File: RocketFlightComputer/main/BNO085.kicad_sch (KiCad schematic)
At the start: 12 parts, among them Y3 32.768kHz

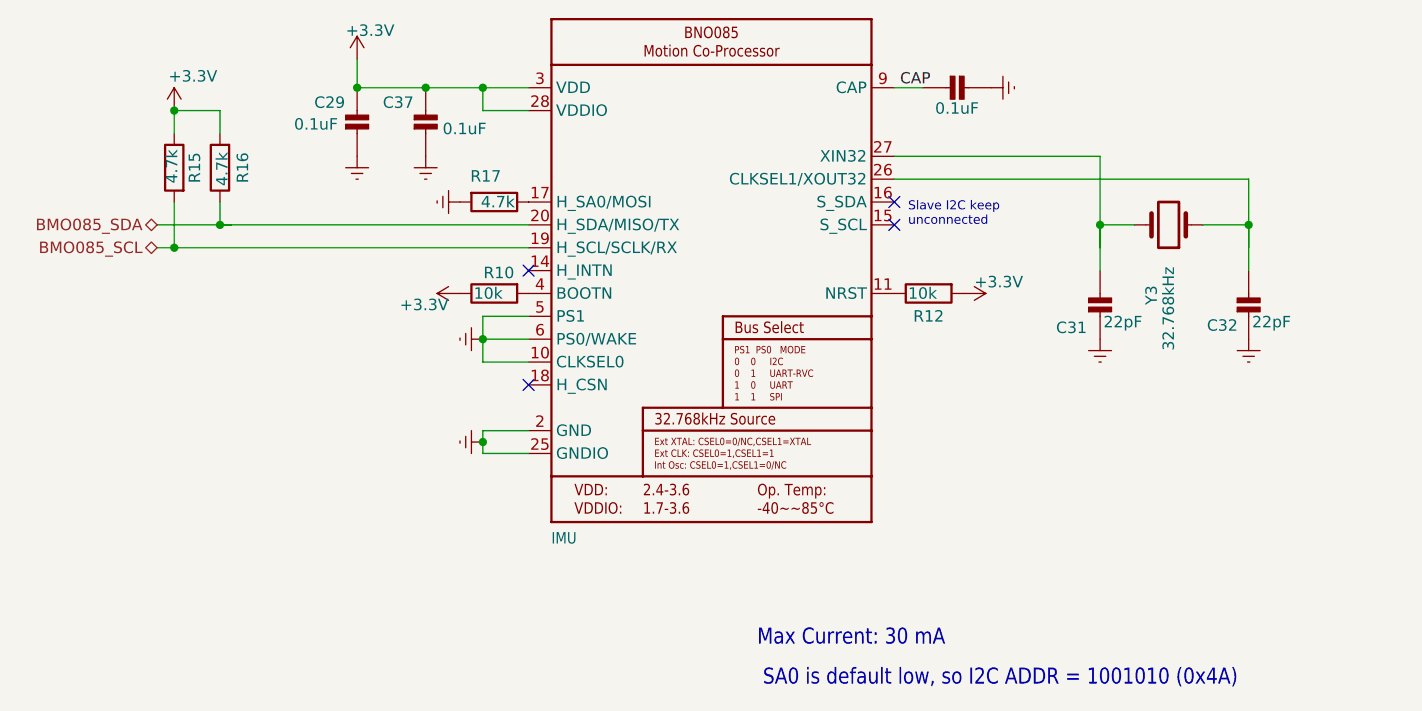
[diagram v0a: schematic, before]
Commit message: Addition of all components in BOM, metal mounting plates, need to check psram if its ok for signals to pass under, all components need a double check
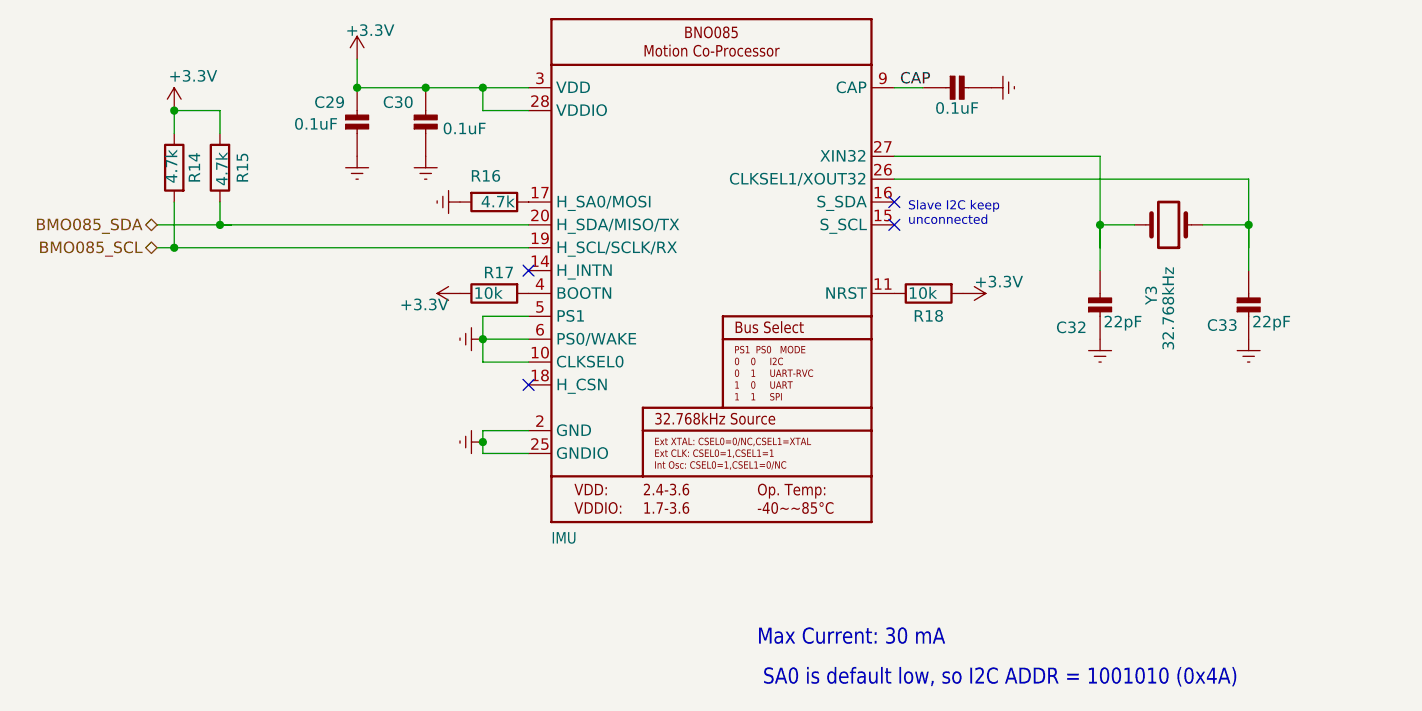
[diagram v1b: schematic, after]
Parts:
- BNO1: renamed from BNO85; LCSC (none) -> C5189642; Mouser Part Number (none) -> 526-BNO085
- C29: LCSC (none) -> C48579250
- C30: renamed from C37; LCSC (none) -> C48579250
- C31: renamed from C30; LCSC (none) -> C48579250
- C32: renamed from C31; LCSC (none) -> C49326308
- C33: renamed from C32; LCSC (none) -> C49326308
- R14: renamed from R15; LCSC (none) -> C23162
- R15: renamed from R16; LCSC (none) -> C23162
- R16: renamed from R17; LCSC (none) -> C23162
- R17: renamed from R10; LCSC (none) -> C25804
- R18: renamed from R12; LCSC (none) -> C25804
- Y3: LCSC (none) -> C1985397; Mouser Part Number (none) -> 815-ABS06-32.7K-1-T

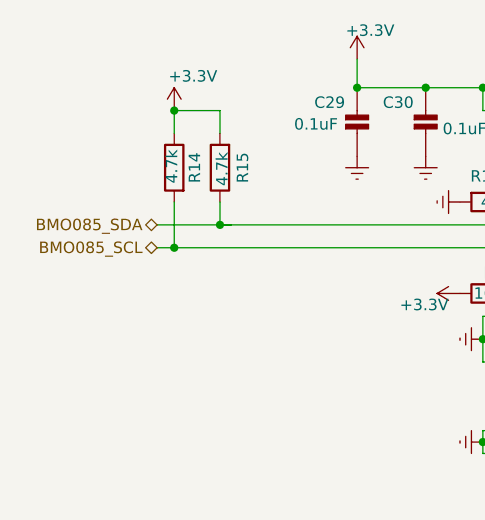
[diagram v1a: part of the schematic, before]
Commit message: First commit with 0.1mm traces and 02mm by 0.43mm vias to fit pcbway standard manufacturing + corrections of PR'S like uart RX of component to TX of mcu
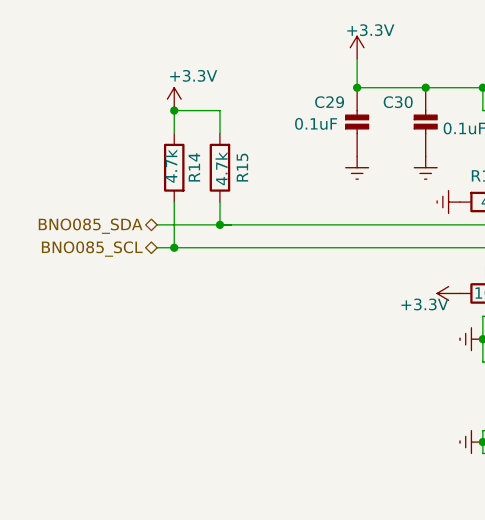
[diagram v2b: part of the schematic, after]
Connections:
- net BMO085_SCL renamed BNO085_SCL
- net BMO085_SDA renamed BNO085_SDA
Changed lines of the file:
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@@
 		)
 	)
-	(hierarchical_label "BMO085_SCL"
+	(hierarchical_label "BNO085_SCL"
 		(shape bidirectional)
 		(at 27.305 54.61 180)
@@
 		)
 	)
-	(hierarchical_label "BMO085_SDA"
+	(hierarchical_label "BNO085_SDA"
 		(shape bidirectional)
 		(at 27.305 52.07 180)

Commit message: Corrected a few subsystems
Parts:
- removed R18: 10k, Resistor_SMD:R_0603_1608Metric_Pad0.98x0.95mm_HandSolder, symbol Device:R
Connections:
- net BNO085_RST: now reaches BNO1.11 (NRST)
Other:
- note added: "CEVA recommends using a crystal with tolerance50ppm with 12.5pF capacitor loading."

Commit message: Corrections of mistake, revision of schematic is done and BOM revised, revision of pcb layout to do
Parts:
- C29, C30, C31: LCSC C48579250 -> C1590
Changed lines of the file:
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@@
 			)
 		)
-		(property "LCSC" "C48579250"
+		(property "LCSC" "C1590"
 			(at 57.15 41.91 0)
 			(hide yes)
@@
 			)
 		)
-		(property "LCSC" "C48579250"
+		(property "LCSC" "C1590"
 			(at 114.935 36.83 0)
 			(hide yes)
@@
 			)
 		)
-		(property "LCSC" "C48579250"
+		(property "LCSC" "C1590"
 			(at 49.53 41.91 0)
 			(hide yes)
